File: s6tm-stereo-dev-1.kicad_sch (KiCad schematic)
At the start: 94 parts, among them J1 Micro_SD_Card_Det1, J2 Conn_01x04_Pin, J3 USB_C_Receptacle_USB2.0_14P, SW1 SW_SPDT, SW2 SW_Push, SW3 SW_Push, SW5 SW_Push, SW6 SW_Push, SW7 RotaryEncoder_Switch, U1 ESP32-S3FN8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

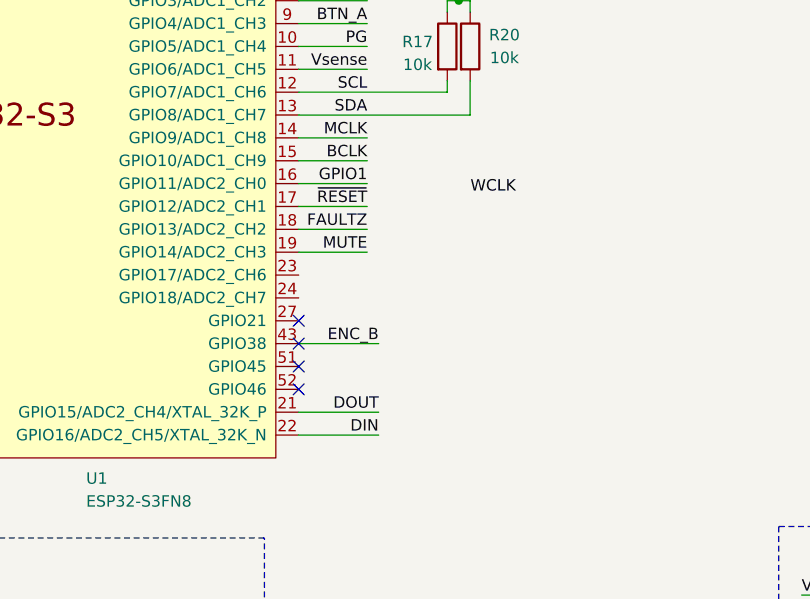
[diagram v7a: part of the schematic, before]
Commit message: pcb: add codec i2s and gpios routing
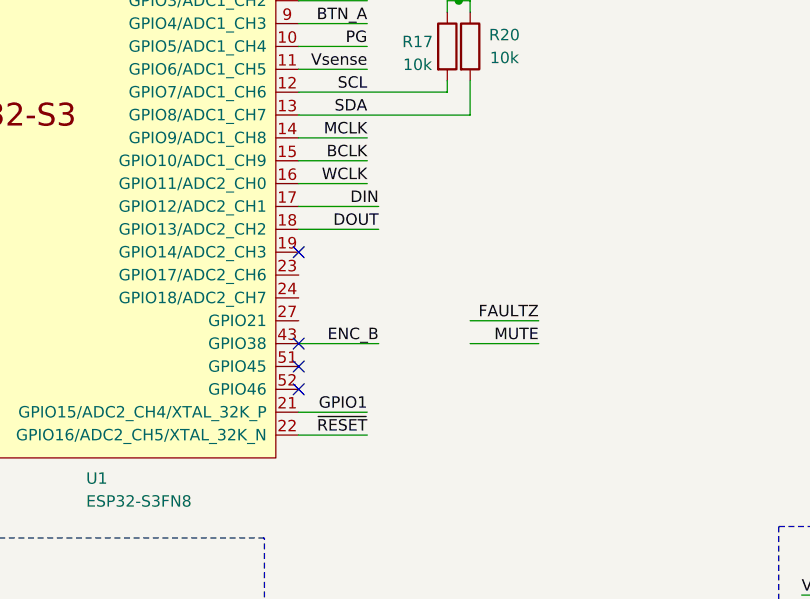
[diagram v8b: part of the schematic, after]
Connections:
- net DIN: now also U1.17 (GPIO12/ADC2_CH1); no longer U1.22 (GPIO16/ADC2_CH5/XTAL_32K_N)
- net DOUT: now also U1.18 (GPIO13/ADC2_CH2); no longer U1.21 (GPIO15/ADC2_CH4/XTAL_32K_P)
- net FAULTZ: no longer U1.18 (GPIO13/ADC2_CH2)
- net GPIO1: now also U1.21 (GPIO15/ADC2_CH4/XTAL_32K_P); no longer U1.16 (GPIO11/ADC2_CH0)
- net MUTE: no longer U1.19 (GPIO14/ADC2_CH3)
- net WCLK: now also U1.16 (GPIO11/ADC2_CH0)
- net ~{RESET}: now also U1.22 (GPIO16/ADC2_CH5/XTAL_32K_N); no longer U1.17 (GPIO12/ADC2_CH1)
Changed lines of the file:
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@@
 	)
 	(no_connect
-		(at 60.96 92.71)
+		(at 127 107.95)
 	)
 	(no_connect
-		(at 127 74.93)
+		(at 60.96 92.71)
 	)
 	(no_connect
-		(at 127 115.57)
+		(at 127 74.93)
 	)
 	(no_connect
@@
 	(wire
 		(pts
-			(xy 134.62 105.41) (xy 127 105.41)
-		)
-		(stroke
-			(width 0)
-			(type default)
-		)
-	)
-	(wire
-		(pts
 			(xy 74.93 176.53) (xy 45.72 176.53)
 		)
@@
 	(wire
 		(pts
-			(xy 134.62 102.87) (xy 127 102.87)
-		)
-		(stroke
-			(width 0)
-			(type default)
-		)
-	)
-	(wire
-		(pts
 			(xy 78.74 31.75) (xy 68.58 31.75)
 		)
@@
 	(wire
 		(pts
+			(xy 127 100.33) (xy 134.62 100.33)
+		)
+		(stroke
+			(width 0)
+			(type default)
+		)
+	)
+	(wire
+		(pts
 			(xy 88.9 21.59) (xy 83.82 21.59)
 		)
@@
 	(wire
 		(pts
+			(xy 153.67 118.11) (xy 146.05 118.11)
+		)
+		(stroke
+			(width 0)
+			(type default)
+		)
+	)
+	(wire
+		(pts
 			(xy 247.65 91.44) (xy 247.65 92.71)
 		)
@@
 	(wire
 		(pts
-			(xy 134.62 100.33) (xy 127 100.33)
-		)
-		(stroke
-			(width 0)
-			(type default)
-		)
-	)
-	(wire
-		(pts
 			(xy 275.59 127) (xy 274.32 127)
 		)
@@
 	(wire
 		(pts
+			(xy 153.67 115.57) (xy 146.05 115.57)
+		)
+		(stroke
+			(width 0)
+			(type default)
+		)
+	)
+	(wire
+		(pts
+			(xy 134.62 128.27) (xy 127 128.27)
+		)
+		(stroke
+			(width 0)
+			(type default)
+		)
+	)
+	(wire
+		(pts
 			(xy 252.73 142.24) (xy 261.62 142.24)
 		)
@@
 	(wire
 		(pts
-			(xy 134.62 107.95) (xy 127 107.95)
-		)
-		(stroke
-			(width 0)
-			(type default)
-		)
-	)
-	(wire
-		(pts
 			(xy 54.61 21.59) (xy 68.58 21.59)
 		)
@@
 	(wire
 		(pts
-			(xy 135.89 128.27) (xy 127 128.27)
-		)
-		(stroke
-			(width 0)
-			(type default)
-		)
-	)
-	(wire
-		(pts
 			(xy 265.43 127) (xy 265.43 128.27)
 		)
@@
 	(wire
 		(pts
-			(xy 135.89 125.73) (xy 127 125.73)
-		)
-		(stroke
-			(width 0)
-			(type default)
-		)
-	)
-	(wire
-		(pts
 			(xy 78.74 30.48) (xy 78.74 31.75)
 		)
@@
 	(wire
 		(pts
+			(xy 135.89 102.87) (xy 127 102.87)
+		)
+		(stroke
+			(width 0)
+			(type default)
+		)
+	)
+	(wire
+		(pts
 			(xy 208.28 146.05) (xy 208.28 147.32)
 		)
@@
 	(wire
 		(pts
+			(xy 135.89 105.41) (xy 127 105.41)
+		)
+		(stroke
+			(width 0)
+			(type default)
+		)
+	)
+	(wire
+		(pts
 			(xy 127 82.55) (xy 134.62 82.55)
 		)
@@
 	(wire
 		(pts
+			(xy 134.62 125.73) (xy 127 125.73)
+		)
+		(stroke
+			(width 0)
+			(type default)
+		)
+	)
+	(wire
+		(pts
 			(xy 35.56 55.88) (xy 35.56 57.15)
 		)
@@
 		)
 	)
-	(label "DIN"
-		(at 135.89 128.27 180)
-		(effects
-			(font
-				(size 1.27 1.27)
-			)
-			(justify right bottom)
-		)
-	)
-	(label "GPIO1"
-		(at 134.62 100.33 180)
-		(effects
-			(font
-				(size 1.27 1.27)
-			)
-			(justify right bottom)
-		)
-	)
 	(label "ESP_D-"
 		(at 135.89 67.31 180)
@@
 		)
 	)
-	(label "MUTE"
-		(at 134.62 107.95 180)
+	(label "D+"
+		(at 148.59 64.77 180)
 		(effects
 			(font
@@
 		)
 	)
-	(label "D+"
-		(at 148.59 64.77 180)
+	(label "MUTE"
+		(at 153.67 118.11 180)
 		(effects
 			(font
@@
 		)
 	)
-	(label "DOUT"
-		(at 135.89 125.73 180)
-		(effects
-			(font
-				(size 1.27 1.27)
-			)
-			(justify right bottom)
-		)
-	)
 	(label "MCLK"
 		(at 173.99 57.15 0)
@@
 	)
 	(label "WCLK"
-		(at 151.13 101.6 180)
+		(at 134.62 100.33 180)
 		(effects
 			(font
@@
 		)
 	)
-	(label "~{RESET}"
-		(at 134.62 102.87 180)
-		(effects
-			(font
-				(size 1.27 1.27)
-			)
-			(justify right bottom)
-		)
-	)
 	(label "BTN_A"
 		(at 134.62 82.55 180)
@@
 		)
 	)
+	(label "DIN"
+		(at 135.89 102.87 180)
+		(effects
+			(font
+				(size 1.27 1.27)
+			)
+			(justify right bottom)
+		)
+	)
 	(label "XTAL_P"
 		(at 52.07 80.01 0)
@@
 		)
 	)
+	(label "GPIO1"
+		(at 134.62 125.73 180)
+		(effects
+			(font
+				(size 1.27 1.27)
+			)
+			(justify right bottom)
+		)
+	)
 	(label "RF_ANT"
 		(at 21.59 35.56 0)
@@
 		)
 	)
+	(label "FAULTZ"
+		(at 153.67 115.57 180)
+		(effects
+			(font
+				(size 1.27 1.27)
+			)
+			(justify right bottom)
+		)
+	)
 	(label "SDA"
 		(at 248.92 62.23 0)
@@
 		)
 	)
+	(label "DOUT"
+		(at 135.89 105.41 180)
+		(effects
+			(font
+				(size 1.27 1.27)
+			)
+			(justify right bottom)
+		)
+	)
 	(label "ENC_A"
 		(at 247.65 33.02 0)
@@
 		)
 	)
-	(label "FAULTZ"
-		(at 134.62 105.41 180)
+	(label "SCL"
+		(at 173.99 44.45 0)
 		(effects
 			(font
 				(size 1.27 1.27)
 			)
-			(justify right bottom)
+			(justify left bottom)
 		)
 	)
-	(label "SCL"
-		(at 173.99 44.45 0)
+	(label "ENC_SW"
+		(at 278.13 33.02 180)
 		(effects
 			(font
 				(size 1.27 1.27)
 			)
-			(justify left bottom)
+			(justify right bottom)
 		)
 	)
-	(label "ENC_SW"
-		(at 278.13 33.02 180)
+	(label "~{RESET}"
+		(at 134.62 128.27 180)
 		(effects
 			(font
